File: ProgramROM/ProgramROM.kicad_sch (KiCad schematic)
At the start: 41 parts, among them J2 Arduino, SW1 SW_DIP_x05, U1 AT28C64, U2 74HC541, U3 74HC595, U4 74HC245, U5 74HC157, U6 74HC04

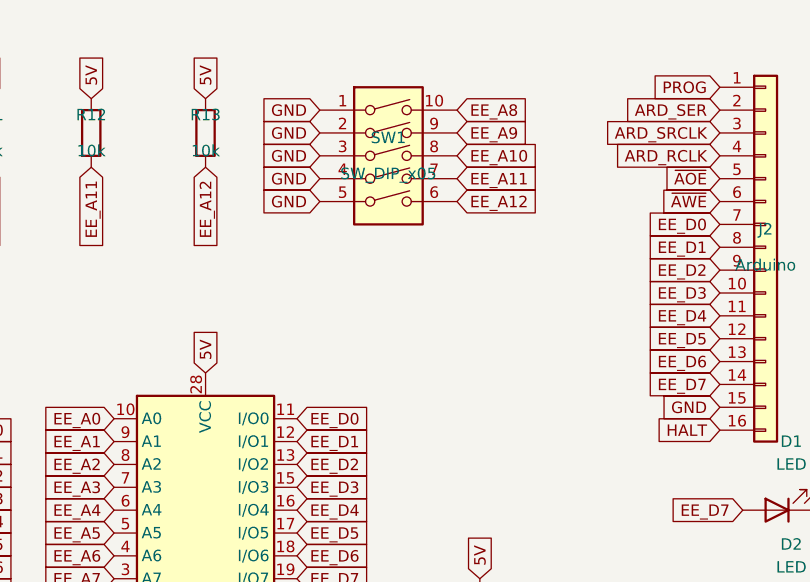
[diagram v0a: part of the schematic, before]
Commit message: [ProgramRom] - added option for future Library bank within the EEProm as described in LibraryBank.md
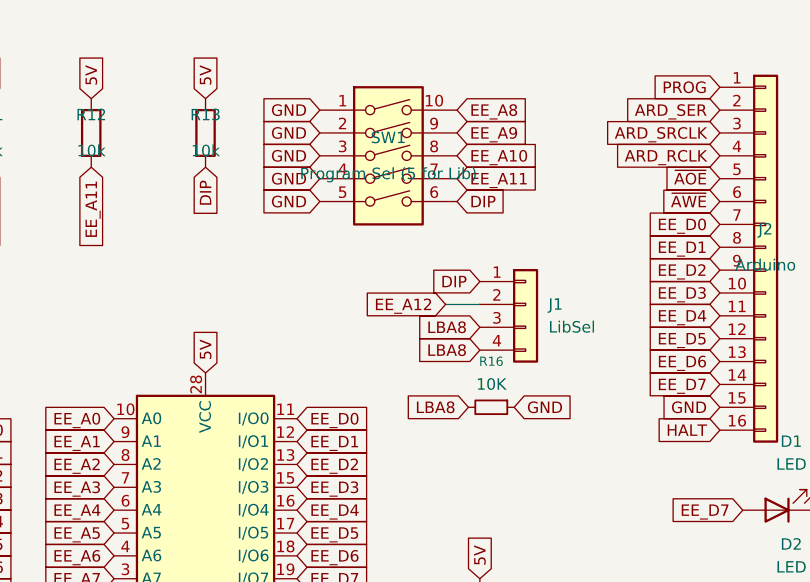
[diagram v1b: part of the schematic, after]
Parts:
- added J1: LibSel, Connector_PinHeader_2.54mm:PinHeader_1x04_P2.54mm_Vertical, symbol Connector_Generic:Conn_01x04
- added R16: 10K, Resistor_SMD:R_0805_2012Metric_Pad1.20x1.40mm_HandSolder, symbol Device:R_Small
- SW1: value SW_DIP_x05 -> Program Sel (5 for Lib)
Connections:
- net EE_A12: now also J1.2 (Pin_2); no longer R13.2, SW1.6
- net GND: now also R16.1
- new net DIP: J1.1 (Pin_1), R13.2, SW1.6
- new net LBA8: J1.3 (Pin_3), J1.4 (Pin_4), R16.2
